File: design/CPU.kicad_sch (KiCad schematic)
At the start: 7 parts, among them J7 Conn_02x32_Odd_Even, U10 MC68010P, Y1 CXO_DIP8 10MHz

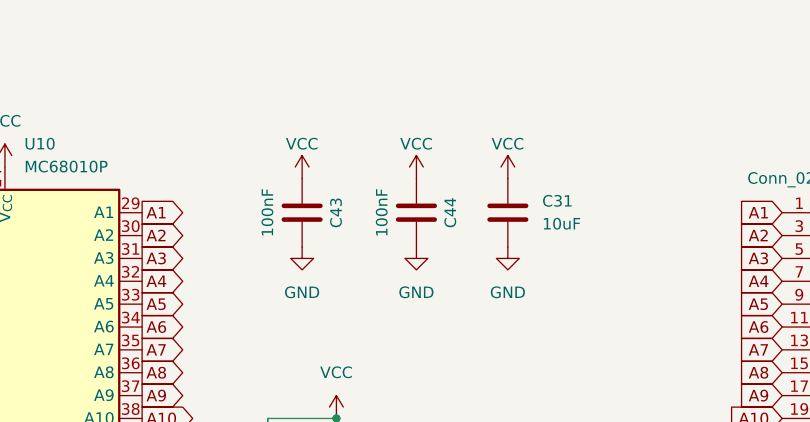
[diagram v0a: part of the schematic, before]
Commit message: Sort out R and C types
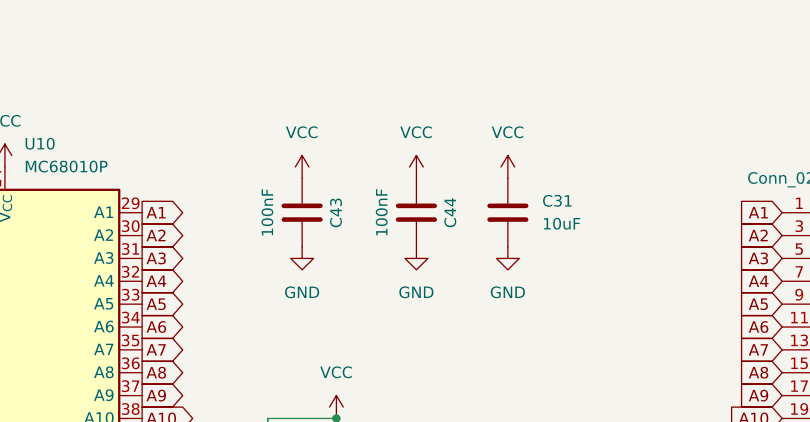
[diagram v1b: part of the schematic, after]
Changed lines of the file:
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@@
-	)
-	(symbol
-		(lib_id "power:VCC")
-		(at 91.44 43.18 0)
-		(unit 1)
-		(body_style 1)
-		(exclude_from_sim no)
-		(in_bom yes)
-		(on_board yes)
-		(in_pos_files yes)
-		(dnp no)
-		(fields_autoplaced yes)
-		(property "Reference" "#PWR057"
-			(at 91.44 46.99 0)
-			(hide yes)
-			(show_name no)
-			(do_not_autoplace no)
-			(effects
-				(font
-					(size 1.27 1.27)
-				)
-			)
-		)
-		(property "Value" "VCC"
-			(at 91.44 39.37 0)
-			(show_name no)
-			(do_not_autoplace no)
-			(effects
-				(font
-					(size 1.27 1.27)
-				)
-			)
-		)
-		(property "Footprint" ""
-			(at 91.44 43.18 0)
-			(hide yes)
-			(show_name yes)
-			(do_not_autoplace no)
-			(effects
-				(font
-					(size 1.27 1.27)
-				)
-			)
-		)
-		(property "Datasheet" ""
-			(at 91.44 43.18 0)
-			(hide yes)
-			(show_name yes)
-			(do_not_autoplace no)
-			(effects
-				(font
-					(size 1.27 1.27)
-				)
-			)
-		)
-		(property "Description" "Power symbol creates a global label with name \"VCC\""
-			(at 91.44 43.18 0)
-			(hide yes)
-			(show_name yes)
-			(do_not_autoplace no)
-			(effects
-				(font
-					(size 1.27 1.27)
-				)
-			)
-		)
-		(pin "1"
-		)
-		(instances
-			(project "Simple010"
-				(path "/4f37455c-e998-4ed3-8493-a94956af64c1/2907fc67-7e28-48cc-93ca-028c1d99c5a1"
-					(reference "#PWR057")
-					(unit 1)
-				)
-			)
-		)
 	)
 	(symbol
@@
 	)
 	(symbol
+		(lib_id "power:VCC")
+		(at 91.44 43.18 0)
+		(unit 1)
+		(body_style 1)
+		(exclude_from_sim no)
+		(in_bom yes)
+		(on_board yes)
+		(in_pos_files yes)
+		(dnp no)
+		(fields_autoplaced yes)
+		(property "Reference" "#PWR01"
+			(at 91.44 46.99 0)
+			(hide yes)
+			(show_name no)
+			(do_not_autoplace no)
+			(effects
+				(font
+					(size 1.27 1.27)
+				)
+			)
+		)
+		(property "Value" "VCC"
+			(at 91.44 38.1 0)
+			(show_name no)
+			(do_not_autoplace no)
+			(effects
+				(font
+					(size 1.27 1.27)
+				)
+			)
+		)
+		(property "Footprint" ""
+			(at 91.44 43.18 0)
+			(hide yes)
+			(show_name no)
+			(do_not_autoplace no)
+			(effects
+				(font
+					(size 1.27 1.27)
+				)
+			)
+		)
+		(property "Datasheet" ""
+			(at 91.44 43.18 0)
+			(hide yes)
+			(show_name no)
+			(do_not_autoplace no)
+			(effects
+				(font
+					(size 1.27 1.27)
+				)
+			)
+		)
+		(property "Description" "Power symbol creates a global label with name \"VCC\""
+			(at 91.44 43.18 0)
+			(hide yes)
+			(show_name no)
+			(do_not_autoplace no)
+			(effects
+				(font
+					(size 1.27 1.27)
+				)
+			)
+		)
+		(pin "1"
+		)
+		(instances
+			(project "Simple010"
+				(path "/4f37455c-e998-4ed3-8493-a94956af64c1/2907fc67-7e28-48cc-93ca-028c1d99c5a1"
+					(reference "#PWR01")
+					(unit 1)
+				)
+			)
+		)
+	)
+	(symbol
 		(lib_name "GND_2")
 		(lib_id "power:GND")
@@
 		(dnp no)
 		(fields_autoplaced yes)
-		(property "Reference" "#PWR083"
+		(property "Reference" "#PWR03"
 			(at 114.3 46.99 0)
 			(hide yes)
@@
 		)
 		(property "Value" "VCC"
-			(at 114.3 39.37 0)
+			(at 114.3 38.1 0)
 			(show_name no)
 			(do_not_autoplace no)
@@
 			(at 114.3 43.18 0)
 			(hide yes)
-			(show_name yes)
+			(show_name no)
 			(do_not_autoplace no)
 			(effects
@@
 			(at 114.3 43.18 0)
 			(hide yes)
-			(show_name yes)
+			(show_name no)
 			(do_not_autoplace no)
 			(effects
@@
 			(at 114.3 43.18 0)
 			(hide yes)
-			(show_name yes)
-			(do_not_autoplace no)
-			(effects
-				(font
-					(size 1.27 1.27)
-				)
-			)
-		)
-		(pin "1"
-		)
-		(instances
-			(project "Simple010"
-				(path "/4f37455c-e998-4ed3-8493-a94956af64c1/2907fc67-7e28-48cc-93ca-028c1d99c5a1"
-					(reference "#PWR083")
+			(show_name no)
+			(do_not_autoplace no)
+			(effects
+				(font
+					(size 1.27 1.27)
+				)
+			)
+		)
+		(pin "1"
+		)
+		(instances
+			(project "Simple010"
+				(path "/4f37455c-e998-4ed3-8493-a94956af64c1/2907fc67-7e28-48cc-93ca-028c1d99c5a1"
+					(reference "#PWR03")
+					(unit 1)
+				)
+			)
+		)
+	)
+	(symbol
+		(lib_id "power:VCC")
+		(at 104.14 43.18 0)
+		(unit 1)
+		(body_style 1)
+		(exclude_from_sim no)
+		(in_bom yes)
+		(on_board yes)
+		(in_pos_files yes)
+		(dnp no)
+		(fields_autoplaced yes)
+		(property "Reference" "#PWR02"
+			(at 104.14 46.99 0)
+			(hide yes)
+			(show_name no)
+			(do_not_autoplace no)
+			(effects
+				(font
+					(size 1.27 1.27)
+				)
+			)
+		)
+		(property "Value" "VCC"
+			(at 104.14 38.1 0)
+			(show_name no)
+			(do_not_autoplace no)
+			(effects
+				(font
+					(size 1.27 1.27)
+				)
+			)
+		)
+		(property "Footprint" ""
+			(at 104.14 43.18 0)
+			(hide yes)
+			(show_name no)
+			(do_not_autoplace no)
+			(effects
+				(font
+					(size 1.27 1.27)
+				)
+			)
+		)
+		(property "Datasheet" ""
+			(at 104.14 43.18 0)
+			(hide yes)
+			(show_name no)
+			(do_not_autoplace no)
+			(effects
+				(font
+					(size 1.27 1.27)
+				)
+			)
+		)
+		(property "Description" "Power symbol creates a global label with name \"VCC\""
+			(at 104.14 43.18 0)
+			(hide yes)
+			(show_name no)
+			(do_not_autoplace no)
+			(effects
+				(font
+					(size 1.27 1.27)
+				)
+			)
+		)
+		(pin "1"
+		)
+		(instances
+			(project "Simple010"
+				(path "/4f37455c-e998-4ed3-8493-a94956af64c1/2907fc67-7e28-48cc-93ca-028c1d99c5a1"
+					(reference "#PWR02")
 					(unit 1)
 				)
@@
 					(unit 1)
 				)
-			)
-		)
-	)
-	(symbol
-		(lib_id "power:VCC")
-		(at 104.14 43.18 0)
-		(unit 1)
-		(body_style 1)
-		(exclude_from_sim no)
-		(in_bom yes)
-		(on_board yes)
-		(in_pos_files yes)
-		(dnp no)
-		(fields_autoplaced yes)
-		(property "Reference" "#PWR059"
-			(at 104.14 46.99 0)
-			(hide yes)
-			(show_name no)
-			(do_not_autoplace no)
-			(effects
-				(font
-					(size 1.27 1.27)
-				)
-			)
-		)
-		(property "Value" "VCC"
-			(at 104.14 39.37 0)
-			(show_name no)
-			(do_not_autoplace no)
-			(effects
-				(font
-					(size 1.27 1.27)
-				)
-			)
-		)
-		(property "Footprint" ""
-			(at 104.14 43.18 0)
-			(hide yes)
-			(show_name yes)
-			(do_not_autoplace no)
-			(effects
-				(font
-					(size 1.27 1.27)
-				)
-			)
-		)
-		(property "Datasheet" ""
-			(at 104.14 43.18 0)
-			(hide yes)
-			(show_name yes)
-			(do_not_autoplace no)
-			(effects
-				(font
-					(size 1.27 1.27)
-				)
-			)
-		)
-		(property "Description" "Power symbol creates a global label with name \"VCC\""
-			(at 104.14 43.18 0)
-			(hide yes)
-			(show_name yes)
-			(do_not_autoplace no)
-			(effects
-				(font
-					(size 1.27 1.27)
-				)
-			)
-		)
-		(pin "1"
-		)
-		(instances
-			(project "Simple010"
-				(path "/4f37455c-e998-4ed3-8493-a94956af64c1/2907fc67-7e28-48cc-93ca-028c1d99c5a1"
-					(reference "#PWR059")
-					(unit 1)
-				)

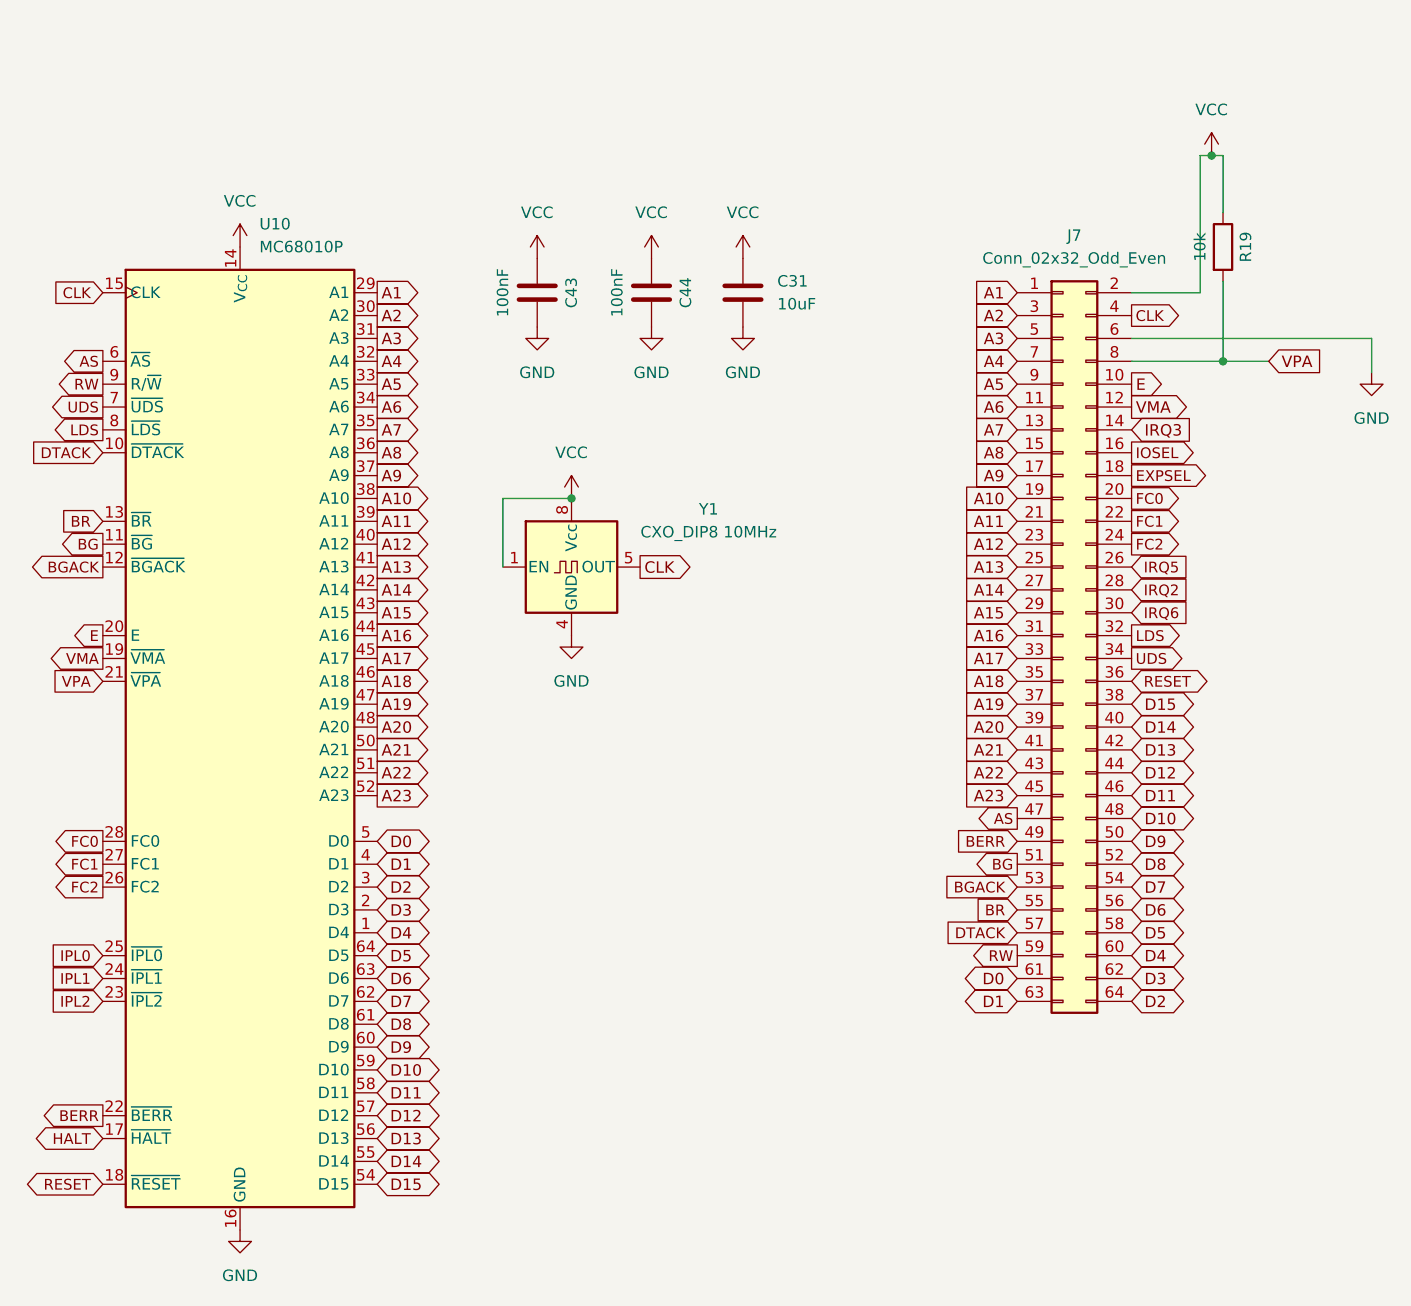
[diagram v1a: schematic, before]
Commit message: Further improvements on CPLD pin placement to improve routing
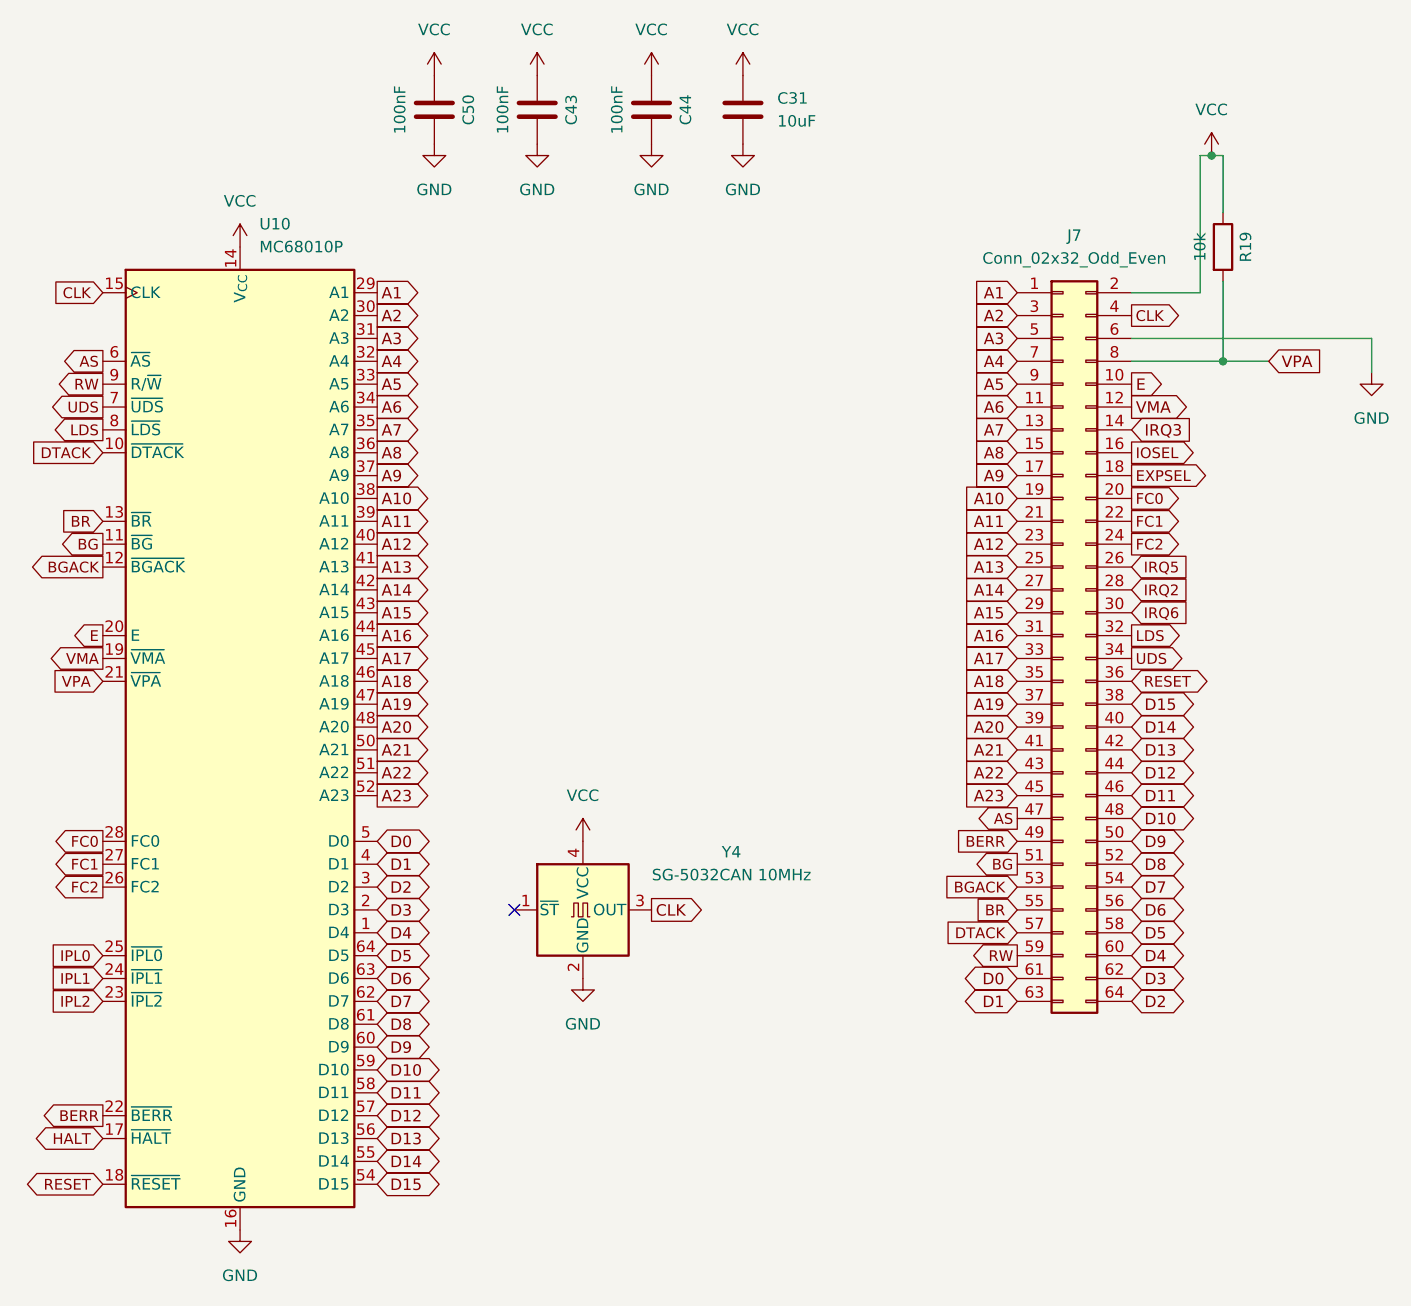
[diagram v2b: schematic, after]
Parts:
- removed Y1: CXO_DIP8 10MHz, Oscillator:Oscillator_DIP-8, symbol Oscillator:CXO_DIP8
- added C50: 100nF, Capacitor_SMD:C_0805_2012Metric_Pad1.18x1.45mm_HandSolder, symbol Device:C
- added Y4: SG-5032CAN 10MHz, Oscillator:Oscillator_SMD_SeikoEpson_SG8002LB-4Pin_5.0x3.2mm_HandSoldering, symbol Oscillator:SG-5032CAN
- J7: footprint (none) -> Connector_PinHeader_2.54mm:PinHeader_2x32_P2.54mm_Vertical
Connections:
- net CLK: now also Y4.3 (OUT)
- net GND: now also C50.2, Y4.2 (GND)
- net VCC: now also C50.1, Y4.4 (VCC)
- no-connect marks 0 -> 1
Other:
- moved on the sheet: C31, C43, C44
